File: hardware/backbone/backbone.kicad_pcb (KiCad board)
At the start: 4 copper layers, 47.9 x 78.2 mm, 172 parts, among them J1 M20-7810645R, J140 M20-7810645R, J2 FROM_PREVIOUS, J3 M20-7810645R, J4 SM04B-SRSS-TB(LF)(SN), J9 TO NEXT, Q2 AO3401A, Q3 AO6604, Q4 AO6604, Q5 AO6604, Q6 AO6604, Q7 AO6604, Q8 AO6604, U1 ESP32-S3-WROOM-1_1U_FlexyPin_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, U12 SN74CBTLV3125PWR, U13 SN74CBTLV3125PWR, U14 AG32VF407VGT6, U16 INA226AIDGSR, U17 74HC4051BQ,115, U18 74HC4051BQ,115, U19 74HC4051BQ,115, U2 SN65HVD230DR, U25 TCA9535PWR(UMW), U3 HC-TYPE-C-16P-01A, U4 TPS562201DDCR, U8 G3VM-61VY3, X1 20MHz

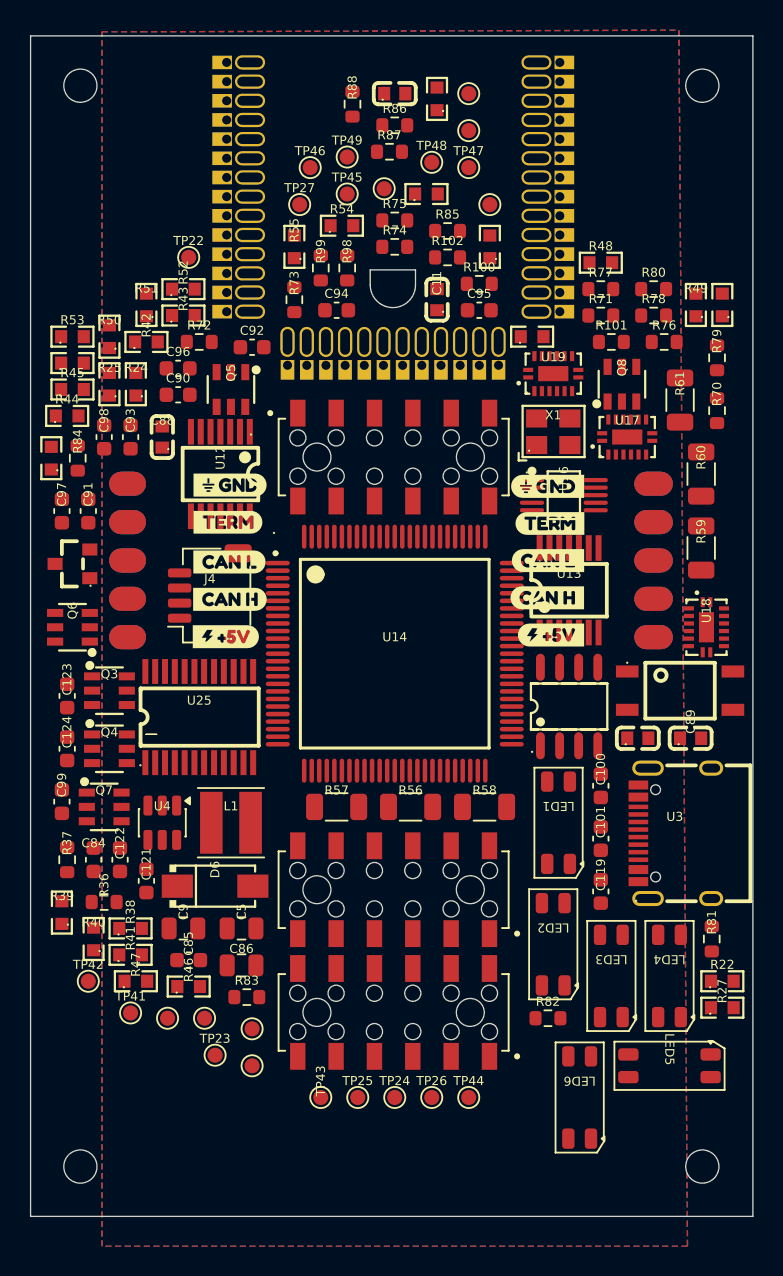
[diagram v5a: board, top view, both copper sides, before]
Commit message: Finalize AG32 backbone layout, sensor pinout and routing setup
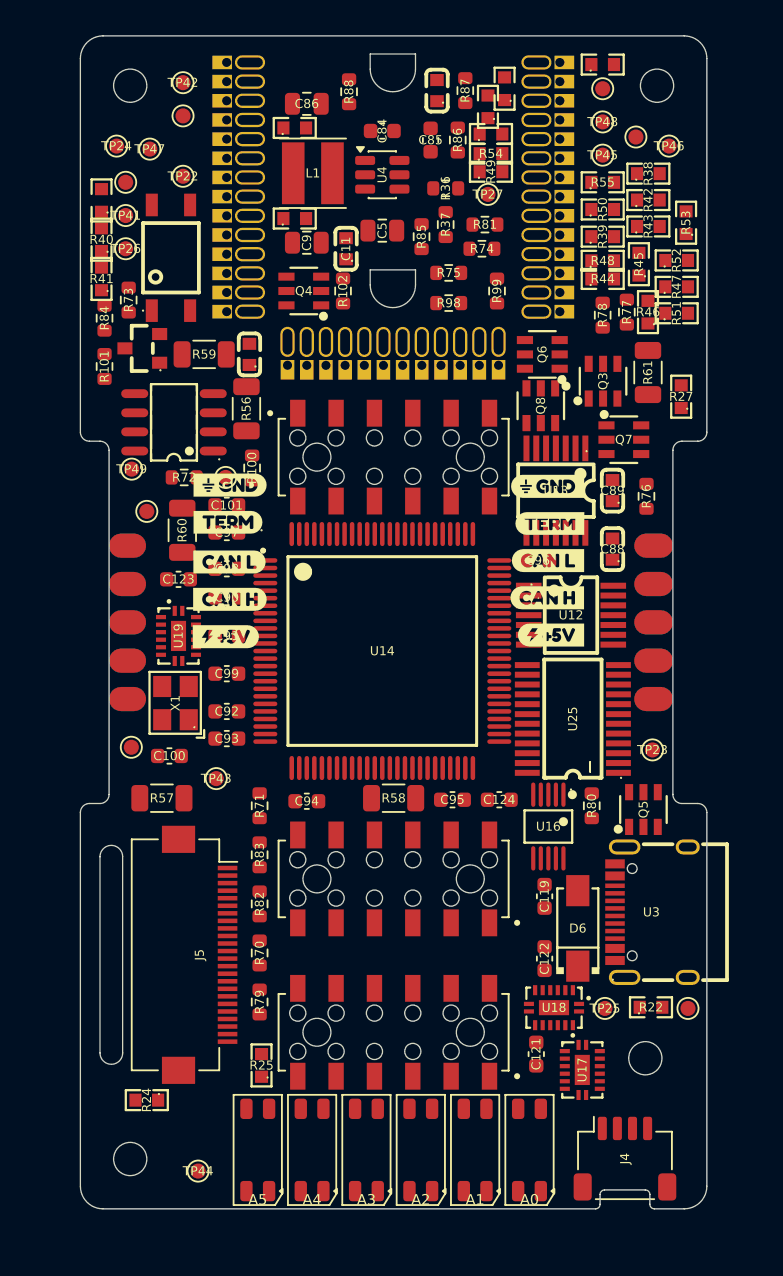
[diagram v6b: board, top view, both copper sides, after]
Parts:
- added J5: FH12-24S-0.5SH(55), SpaghettiLAB:Hirose_FH12-24S-0.5SH_1x24-1MP_P0.50mm_Horizontal, F.Cu at (154.9, 123.2)
- moved TP24 65.7 mm to (149.4, 69.6)
- moved TP12 64.3 mm to (183.8, 69.0)
- moved R38 60.6 mm to (184.6, 71.4)
- moved TP42 59.9 mm to (153.8, 65.4)
- moved TP26 59.8 mm to (150.0, 76.4)
- moved R47 58.3 mm to (186.5, 78.9)
- moved R39 57.3 mm to (181.6, 75.6), turned to 0 degrees
- moved C86 57.2 mm to (162.0, 66.8)
- moved C85 56.6 mm to (170.2, 69.2), turned to 90 degrees
- moved R46 54.1 mm to (184.6, 80.6), turned to 90 degrees
- moved TP41 52.8 mm to (150.0, 74.2)
- moved R36 52.4 mm to (171.2, 72.4), turned to 180 degrees
- moved R79 52.3 mm to (158.9, 126.3)
- moved C84 51.9 mm to (167.0, 68.6), turned to 180 degrees
- moved R81 49.7 mm to (173.8, 74.8), turned to 0 degrees
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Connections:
- net /AG_USB_DM renamed /USB_AG_D-
- net /AG_USB_DP renamed /USB_AG_D+
- net Net-(U19-USB_D+) renamed USB_ESP_D+
- net Net-(U19-USB_D-) renamed USB_ESP_D-
- J3 pad 1: VCORE -> A1
- J3 pad 10: GND -> A3
- J3 pad 11: A4 -> VCORE
- J3 pad 12: A5 -> A2
- J3 pad 2: GND -> VCORE
- J3 pad 3: A0 -> VCORE
- J3 pad 4: A1 -> GND
- J3 pad 5: VCORE -> GND
- J3 pad 6: GND -> A5
- J3 pad 7: A2 -> A0
- J3 pad 8: A3 -> A4
- J3 pad 9: VCORE -> GND
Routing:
- added copper zone on In1.Cu, net GND
- removed copper zone on In1.Cu, net 5V
- removed copper zone on B.Cu, net GND
- removed copper zone on F.Cu, net GND
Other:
- board size 47.9 x 78.2 mm -> 41.5 x 77.7 mm
- board text added: "3V3"
- board text added: "A0"
- board text added: "A1"
- board text added: "A2"
- board text added: "A3"
- board text added: "A4"
- board text added: "A5"
- board text added: "GND"
- board text added: "IO1"
- board text added: "IO10"
- board text added: "IO2"
- board text added: "IO7"
- board text added: "IO8"
- board text added: "IO9"
- board text added: "P1"
- board text added: "P2"
- board text added: "P3"
- board text added: "P4"
- board text added: "P5"
- board text added: "P6"
- board text added: "RGB LEDs (TOP)"

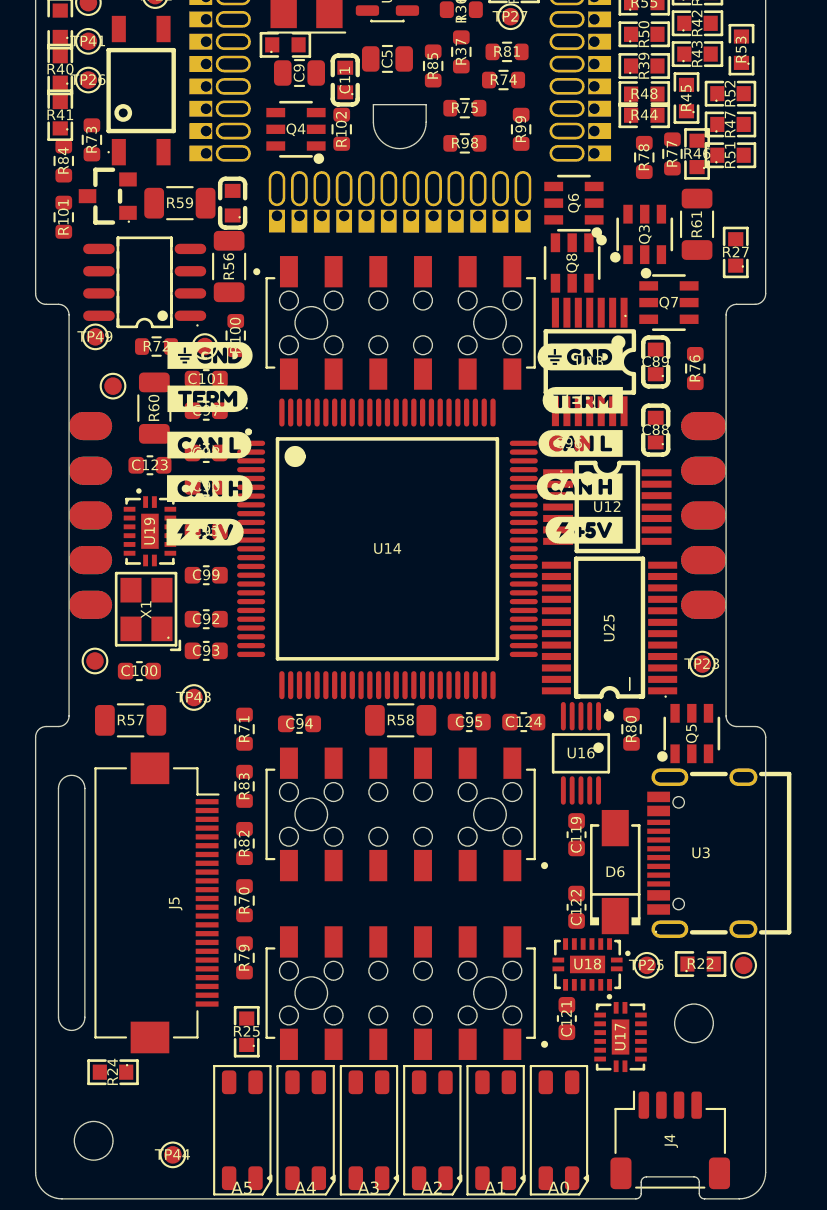
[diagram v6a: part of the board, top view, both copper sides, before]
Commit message: Support ESP32 or AG32 ownership of CAN, LEDs and configurable ports
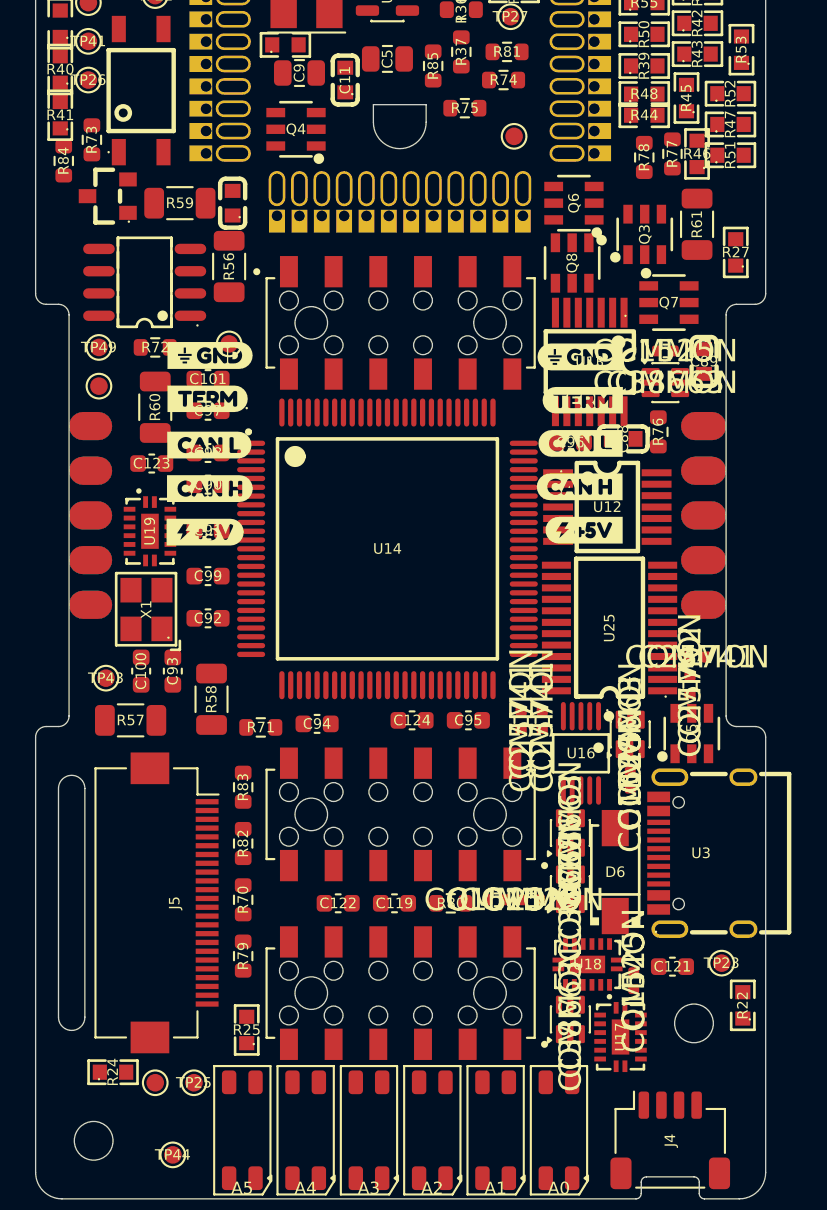
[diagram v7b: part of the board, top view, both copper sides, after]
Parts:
- removed R100, R101, R102, R98, R99: 0R / ESP-only, Resistor_SMD:R_0603_1608Metric
- added C125: 100nF, Capacitor_SMD:C_0402_1005Metric, F.Cu at (180.8, 116.2)
- added C126: 100nF, Capacitor_SMD:C_0402_1005Metric, F.Cu at (175.2, 123.0)
- added C127: 100nF, Capacitor_SMD:C_0402_1005Metric, F.Cu at (173.2, 123.0)
- added C128: 100nF, Capacitor_SMD:C_0402_1005Metric, F.Cu at (181.0, 127.6)
- added C129: 100nF, Capacitor_SMD:C_0402_1005Metric, F.Cu at (182.8, 91.8)
- added R103: 100k, Resistor_SMD:R_0402_1005Metric, F.Cu at (175.8, 112.8)
- added R104: 47k, Resistor_SMD:R_0402_1005Metric, F.Cu at (184.2, 110.8)
- added R105: 100k, Resistor_SMD:R_0402_1005Metric, F.Cu at (184.6, 109.2)
- added R106: 100k, Resistor_SMD:R_0402_1005Metric, F.Cu at (174.6, 112.8)
- added U26: SN74LVC1G3157DCKR, Package_TO_SOT_SMD:SOT-363_SC-70-6, F.Cu at (180.8, 113.6)
- added U27: SN74LVC1G3157DCKR, Package_TO_SOT_SMD:SOT-363_SC-70-6, F.Cu at (177.4, 119.2)
- added U28: SN74LVC1G3157DCKR, Package_TO_SOT_SMD:SOT-363_SC-70-6, F.Cu at (177.4, 122.4)
- added U29: SN74LVC1G3157DCKR, Package_TO_SOT_SMD:SOT-363_SC-70-6, F.Cu at (177.4, 129.8)
- added U30: SN74LVC1G3157DCKR, Package_TO_SOT_SMD:SOT-363_SC-70-6, F.Cu at (182.8, 93.6)
- moved TP21 34.1 mm to (153.8, 133.4)
- moved TP13 26.9 mm to (174.2, 79.6)
- moved TP25 26.6 mm to (156.0, 133.4)
- moved TP23 17.0 mm to (186.0, 126.6)
- moved TP15 15.6 mm to (150.6, 93.8)
- moved R80 14.3 mm to (170.6, 123.2), turned to 0 degrees
- moved C122 13.6 mm to (164.2, 123.2), turned to 0 degrees
- moved C119 11.1 mm to (167.4, 123.2), turned to 0 degrees
- moved R58 10.8 mm to (157.0, 111.6), turned to 90 degrees
- moved C121 6.69 mm to (183.2, 126.8), turned to 0 degrees
- moved C124 6.35 mm to (168.4, 112.8), turned to 0 degrees
- moved TP43 5.12 mm to (151.0, 110.4)
- moved R76 4.17 mm to (182.4, 96.4)
- moved R22 3.36 mm to (187.2, 129.0), turned to 90 degrees
- moved C89 2.75 mm to (185.0, 92.4)
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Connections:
- net IO17 renamed ESP_CAN_TX
- net IO21 renamed ESP_LED_DATA
- net IO38 renamed ESP_TERM_CTRL
- net IO39 renamed ESP_ISO4_N
- net IO40 renamed ESP_ISO5_N
- J5 pad 8: IO18 -> CAN_RX
- U1 pad 11: IO18 -> CAN_RX
- U14 pad 1: TERM_CTRL -> AG_TERM_CTRL
- U14 pad 35: ISO_A4_N -> AG_ISO4_N
- U14 pad 36: ISO_A5_N -> AG_ISO5_N
- U14 pad 52: P_GATE_0 -> AG_READY
- U14 pad 53: N_GATE_0 -> (no net)
- U14 pad 54: P_GATE_1 -> (no net)
- U14 pad 55: N_GATE_1 -> (no net)
- U14 pad 56: P_GATE_2 -> (no net)
- U14 pad 57: N_GATE_2 -> (no net)
- U14 pad 58: P_GATE_3 -> (no net)
- U14 pad 59: N_GATE_3 -> (no net)
- U14 pad 60: P_GATE_4 -> (no net)
- U14 pad 61: N_GATE_4 -> (no net)
- U14 pad 62: P_GATE_5 -> (no net)
- U14 pad 63: N_GATE_5 -> (no net)
- U14 pad 64: ISO_A0_N -> (no net)
- U14 pad 65: ISO_A1_N -> (no net)
- U14 pad 66: ISO_A2_N -> (no net)
- U14 pad 67: ISO_A3_N -> (no net)
- U14 pad 7: ALED -> AG_LED_DATA
- U14 pad 92: CAN_TX -> AG_CAN_TX

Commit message: Share INA226 and current mux control between ESP32 and AG32; expose external SPI
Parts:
- added R107: 10k, Resistor_SMD:R_0402_1005Metric, F.Cu at (166.1, 112.9)
- added R108: 100k, Resistor_SMD:R_0402_1005Metric, F.Cu at (156.8, 108.5)
- R70: value 100k -> 10k
- R79, R80: value 4.7k -> 10k
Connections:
- net IO11 renamed EXT_SPI_CS_N
- J5 pad 15: IO41 -> MEAS_S2
- J5 pad 16: IO42 -> MEAS_INHIBIT
- J5 pad 19: /SPARE_IO_17 -> CTRL14
- J5 pad 20: /SPARE_IO_33 -> SPI_MOSI
- J5 pad 21: /SPARE_IO_34 -> SPI_MISO
- J5 pad 3: IO6 -> MEAS_S0
- J5 pad 5: IO12 -> MEAS_S1
- R70 pad 2: /MEAS_INHIBIT -> MEAS_INHIBIT
- R79 pad 2: /INA_SDA -> MEAS_S0
- R80 pad 2: /INA_SCL -> MEAS_S1
- U1 pad 20: IO12 -> MEAS_S1
- U1 pad 34: IO41 -> MEAS_S2
- U1 pad 35: IO42 -> MEAS_INHIBIT
- U1 pad 6: IO6 -> MEAS_S0
- U14 pad 2: /MEAS_S0 -> MEAS_S0
- U14 pad 3: /MEAS_S1 -> MEAS_S1
- U14 pad 4: /MEAS_S2 -> MEAS_S2
- U14 pad 5: /MEAS_INHIBIT -> MEAS_INHIBIT
- U14 pad 82: /INA_SDA -> (no net)
- U14 pad 83: /INA_SCL -> (no net)
- U16 pad 4: /INA_SDA -> IO4
- U16 pad 5: /INA_SCL -> IO5
- U17 pad 10: /MEAS_S1 -> MEAS_S1
- U17 pad 11: /MEAS_S0 -> MEAS_S0
- U17 pad 6: /MEAS_INHIBIT -> MEAS_INHIBIT
- U17 pad 9: /MEAS_S2 -> MEAS_S2
- U18 pad 10: /MEAS_S1 -> MEAS_S1
- U18 pad 11: /MEAS_S0 -> MEAS_S0
- U18 pad 6: /MEAS_INHIBIT -> MEAS_INHIBIT
- U18 pad 9: /MEAS_S2 -> MEAS_S2
